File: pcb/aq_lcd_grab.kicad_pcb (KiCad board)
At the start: 4 copper layers, 32 x 50 mm, 41 parts, among them J1 Conn_01x39_Socket, J2 Conn_01x39_Socket, J3 Conn_01x03_Socket, J4 Conn_01x04_Socket, J5 Conn_01x03_Pin, U1 RP2350_60QFN, U2 Conn_01x14, Y1 ABM8-272-T3

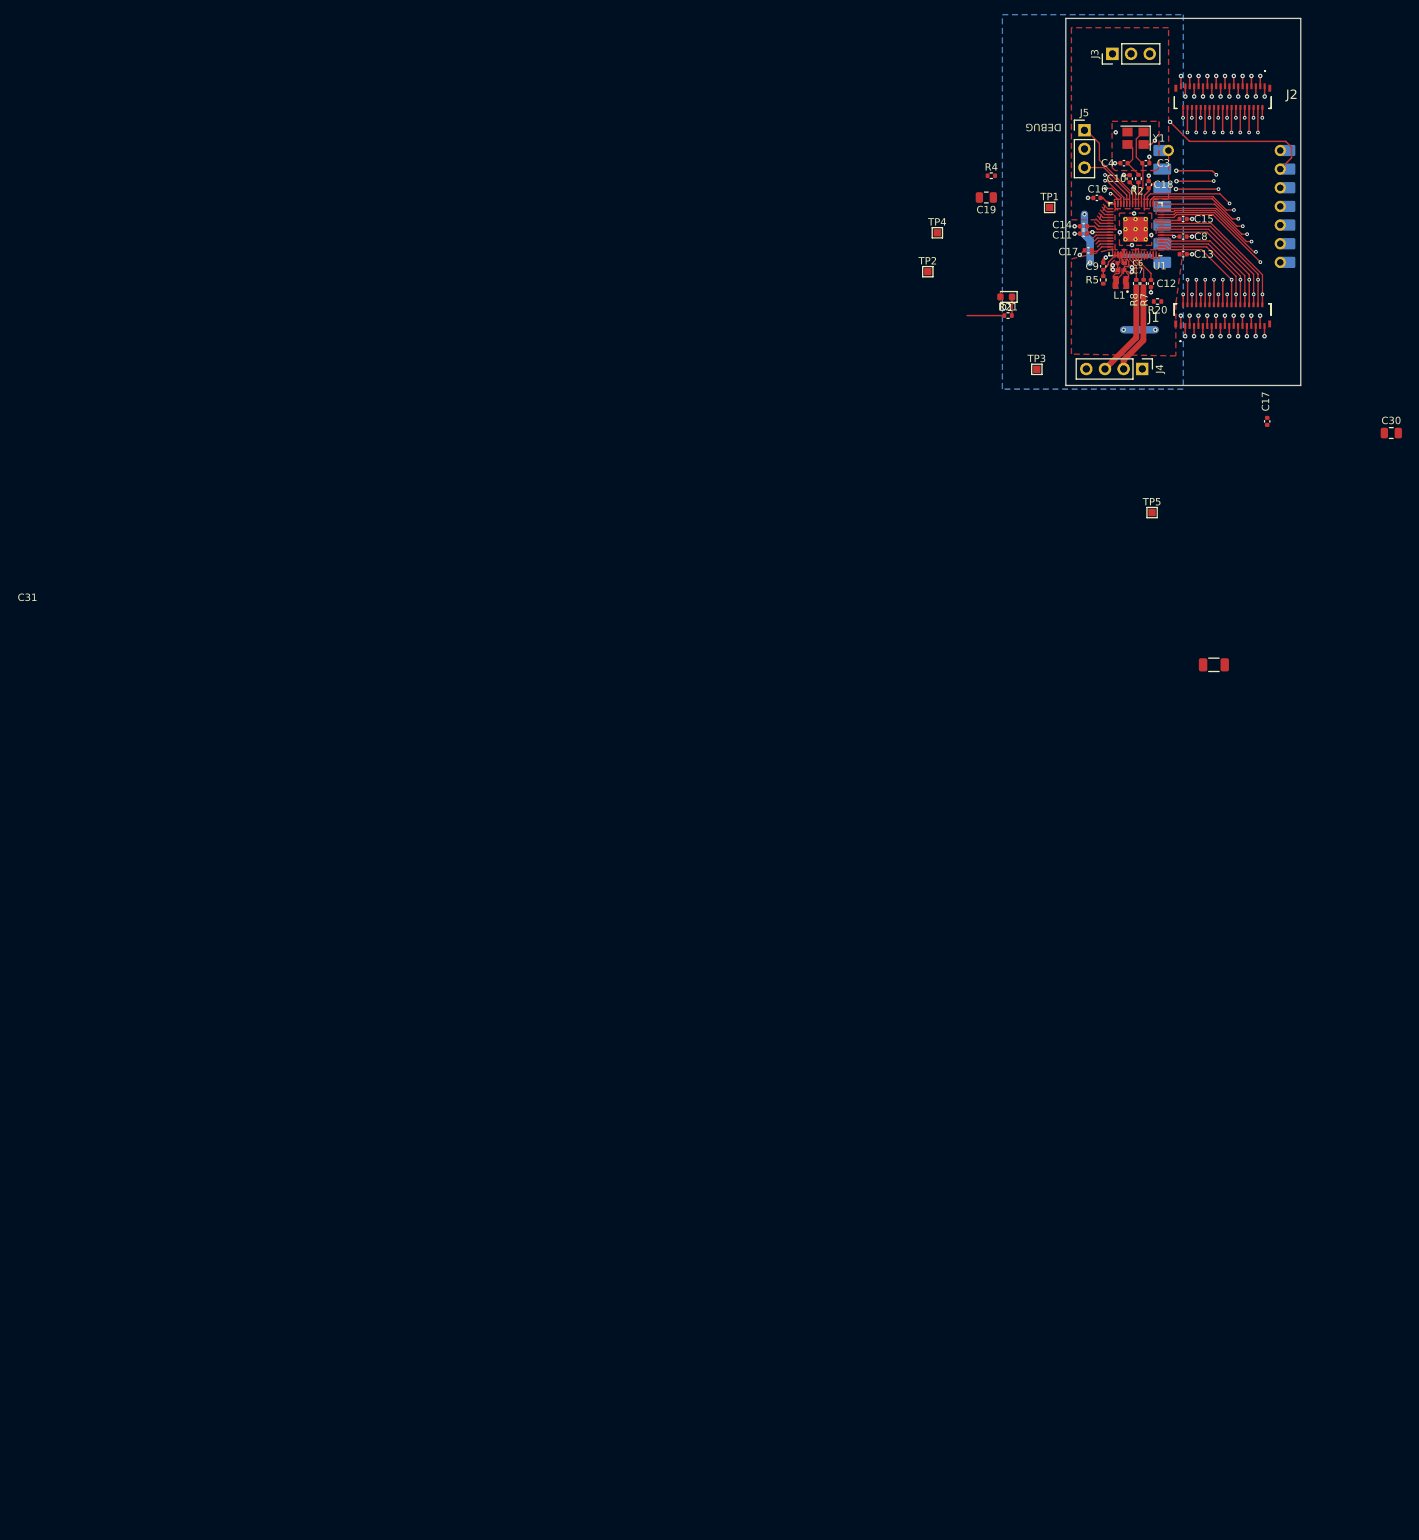
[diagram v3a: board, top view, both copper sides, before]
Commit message: Re-import netlist into PCB
Picks up the smaller test point footprint and the named QSPI strap
nets from the previous commit, plus accumulated layout-side work
from the KiCad session (component placement, routing in progress).

Co-Authored-By: Claude Opus 4.7 (1M context) <noreply@anthropic.com>
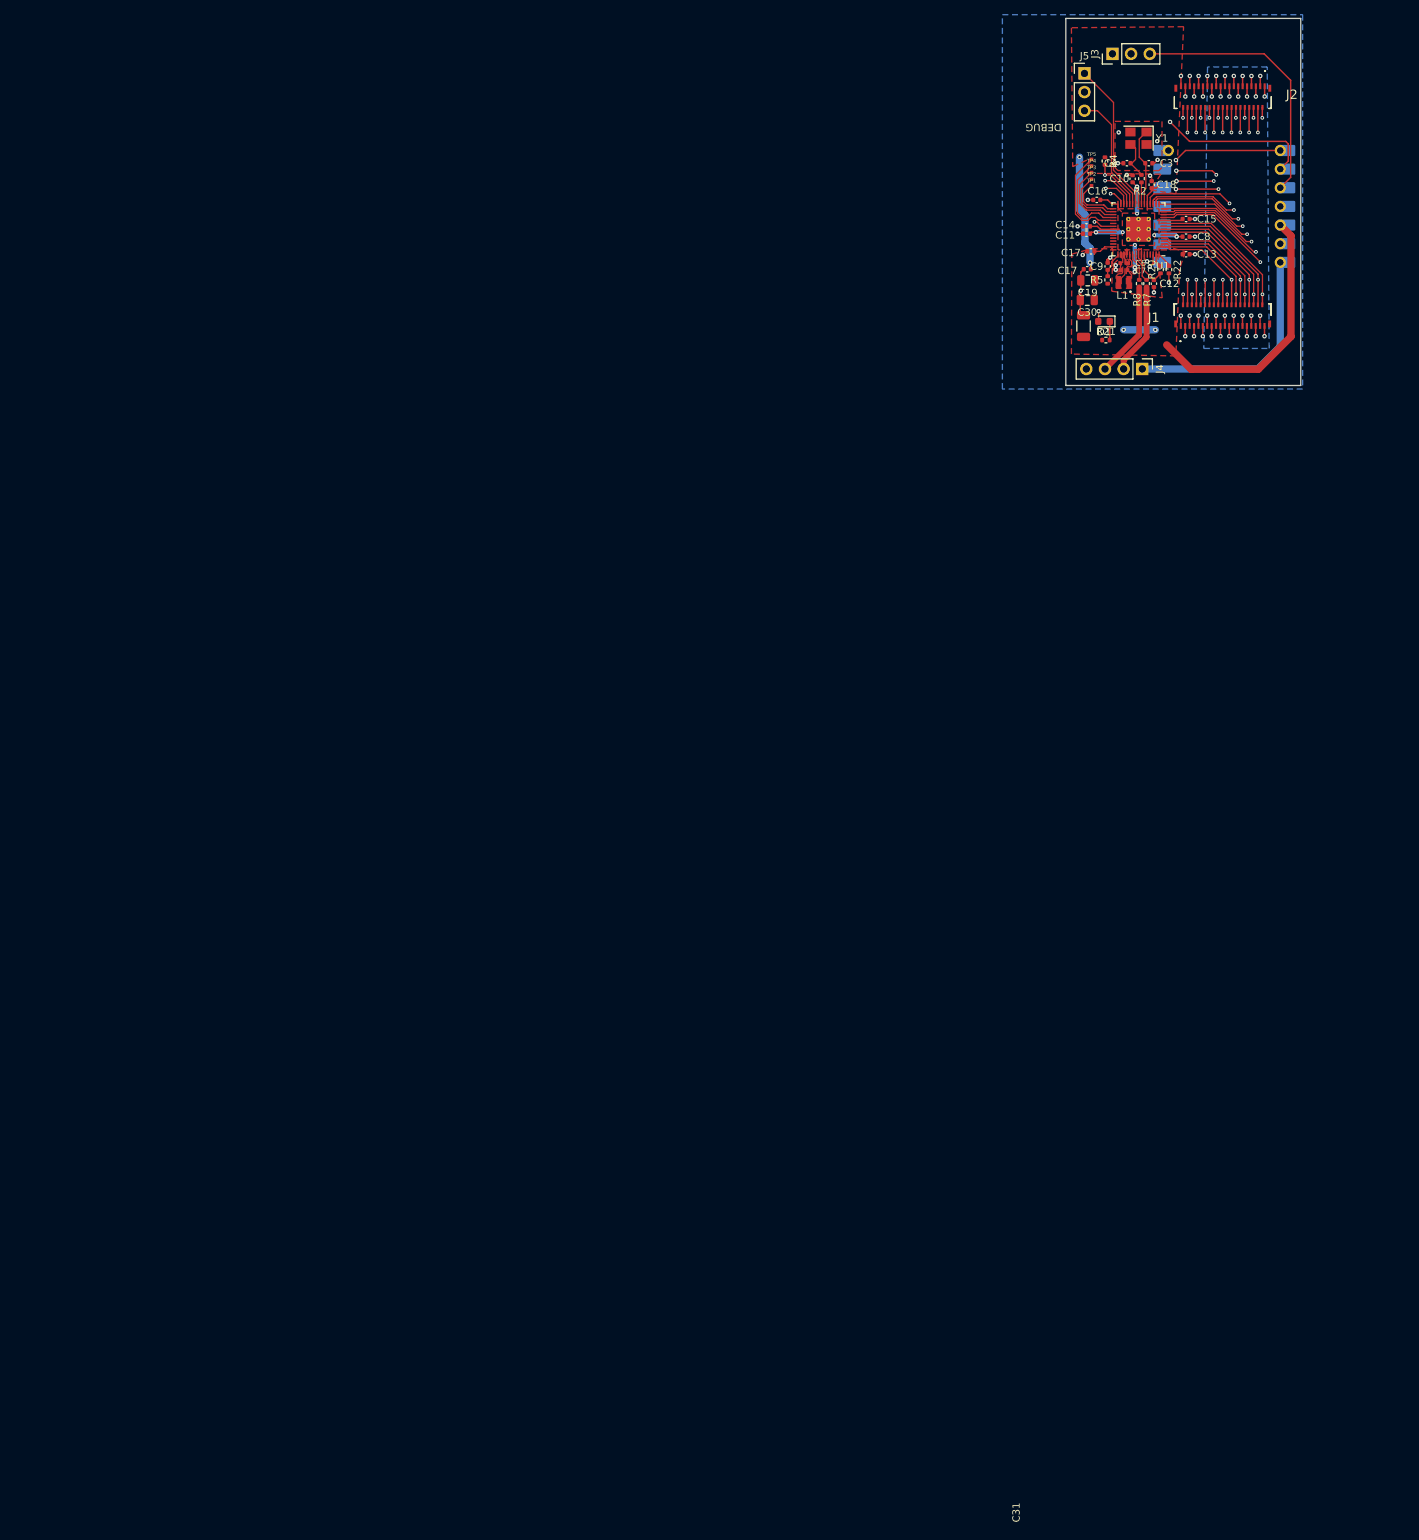
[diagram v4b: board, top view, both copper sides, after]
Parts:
- added R22: 0, Resistor_SMD:R_0402_1005Metric, F.Cu at (64.8, 59.6)
- TP1, TP2, TP3, TP4, TP5: footprint TestPoint:TestPoint_Pad_1.0x1.0mm -> test_points:TestPoint_Pad_0.5x0.5mm
- moved C31 49.4 mm to (53.2, 67.3), turned to 90 degrees
- moved TP5 48.8 mm to (54.3, 44.6)
- moved C30 45.2 mm to (53.7, 63.8), turned to 180 degrees
- moved C17 32.1 mm to (53.7, 59.6), turned to 180 degrees
- moved TP3 27.8 mm to (54.3, 46.4)
- moved TP2 25.6 mm to (54.3, 47.3)
- moved TP4 22.9 mm to (54.3, 45.5)
- moved C19 17.8 mm to (53.8, 61.1)
- moved R4 15.6 mm to (56.1, 44.8), turned to -90 degrees
- moved R21 13.7 mm to (56.3, 69.2)
- moved D1 13.7 mm to (56.0, 66.7)
- moved J5 7.75 mm to (53.3, 32.9)
- moved TP1 6.42 mm to (54.3, 48.2)
- moved R20 4.37 mm to (63.7, 59.6), turned to 90 degrees
- moved C9 0.60 mm to (56.5, 59.2)
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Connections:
- R20 pad 2: N$1 (its old number) -> QSPI_SD1_STRAP
- U1 pad 59: N$1 (its old number) -> QSPI_SD1_STRAP
- U1 pad 60: GND -> QSPI_SS_STRAP
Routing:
- net +3V3: track 41.7 -> 83.7 mm
- net PIC32_RESET: track 0.00 -> 35.9 mm
- net UART_RP_TX: track 0.46 -> 32.6 mm, vias 0 -> 2
- net +5V: track 0.00 -> 31.5 mm
- net UART_RP_RX: track 0.76 -> 17.4 mm, vias 0 -> 1
- net LED_STATUS: track 3.03 -> 16.5 mm, vias 0 -> 2
- net GPIO23: track 2.01 -> 13.8 mm
- net (no net): track 11.1 -> 0.00 mm
- net GPIO22: track 1.81 -> 12.5 mm
- net +1V1: track 14.6 -> 25.1 mm, vias 5 -> 9
- net GPIO21: track 1.61 -> 9.69 mm
- net SWCLK: track 12.9 -> 20.7 mm
- net SWDIO: track 9.07 -> 16.5 mm
- net GPIO20: track 1.36 -> 8.17 mm
- net GPIO19: track 1.21 -> 7.00 mm
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
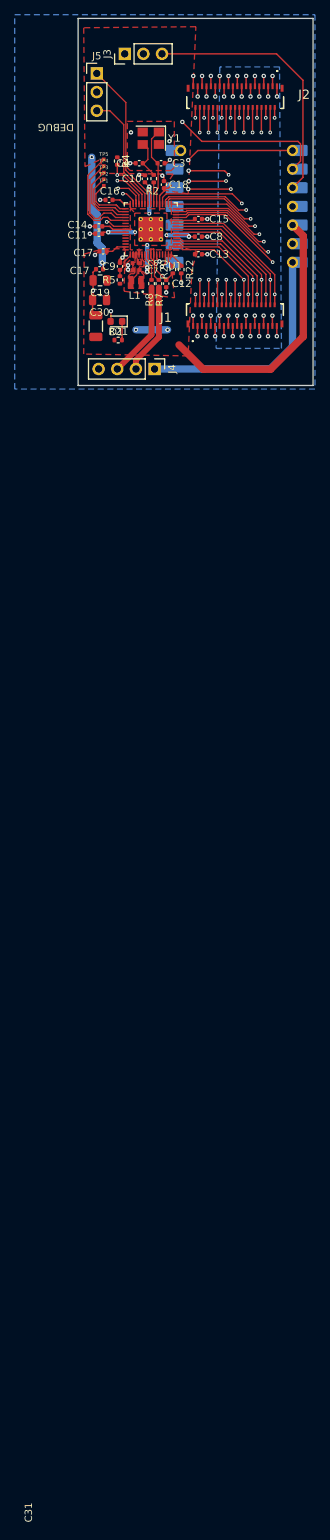
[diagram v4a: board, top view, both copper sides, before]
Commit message: Swap RP2350 for STM32: spec to F103C8T6, PCB rewrite still on F030
docs/pcb_spec.md: rewrite from the RP2350 + flashless UART-boot plan
to STM32. Settle on STM32F103C8T6 after a brief detour through
STM32F030C8T6 (kept as an in-spec addendum for the reasoning trail).
Capture path moves from PIO + DMA ring to TIM1_ETR clocked from WR
with multi-channel DMA reads of GPIOA/GPIOB; channel-to-event
mapping verified against RM0008 Table 78. Pin map handles the F103
specifics: USART1 permanently on PA9/PA10 (bootloader + runtime),
SWD on PA13/PA14, TIM1_ETR on PA12, BOOT1=PB2 forces a pull-down
and moves the status LED off that pin.

pcb/: SKiDL netlist + KiCad PCB + netlist file are an in-progress
F030C8T6 rewrite from a prior session. Committed as-is for history;
they don't yet reflect the F103 decision in the spec and will need
another pass.

.gitignore: stop tracking pcb/production/ fab-output dumps.

Co-Authored-By: Claude Opus 4.7 (1M context) <noreply@anthropic.com>
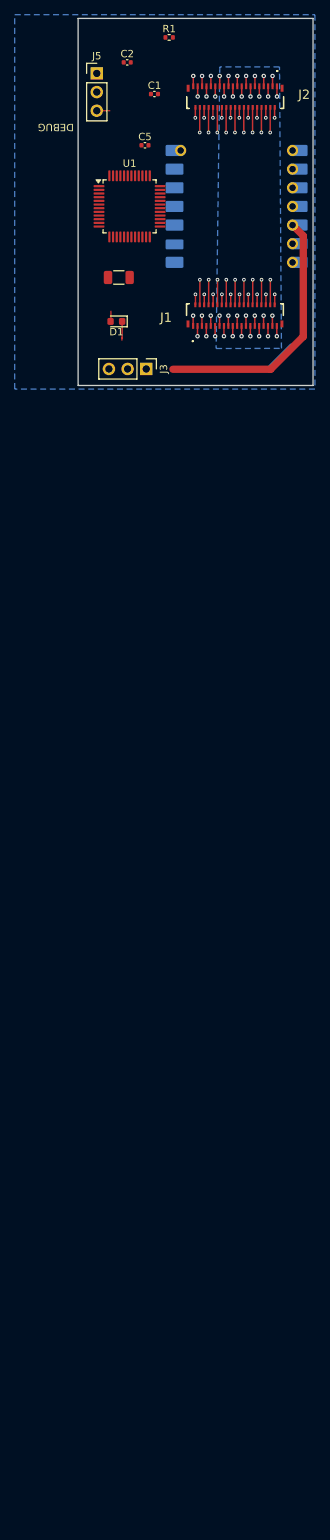
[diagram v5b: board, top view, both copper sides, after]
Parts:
- removed C10, C9: 4.7u, Capacitor_SMD:C_0402_1005Metric
- removed C12, C13, C14, C15, C16, C17 (x2), C18, C8: 100n, Capacitor_SMD:C_0402_1005Metric
- removed C19: 10u, Capacitor_SMD:C_0805_2012Metric
- removed C3, C4: 15p, Capacitor_SMD:C_0402_1005Metric
- removed C30: 22u, Capacitor_SMD:C_0805_2012Metric
- removed C31: 100u, Capacitor_SMD:C_1206_3216Metric
- removed C6, C7: 4.7u, RP2350_60QFN_minimal:C_0402_1005Metric_small_pads
- removed J4: Conn_01x04_Socket, Connector_PinHeader_2.54mm:PinHeader_1x04_P2.54mm_Vertical
- removed L1: 3.3u, RP2350_60QFN_minimal:L_pol_2016
- removed R2, R20, R21, R4: 1k, Resistor_SMD:R_0402_1005Metric
- removed R22: 0, Resistor_SMD:R_0402_1005Metric
- removed R5: 33, Resistor_SMD:R_0402_1005Metric
- removed R7, R8: 27, Resistor_SMD:R_0402_1005Metric
- removed TP1, TP2, TP3, TP4, TP5: TestPoint, test_points:TestPoint_Pad_0.5x0.5mm
- removed Y1: ABM8-272-T3, Crystal:Crystal_SMD_3225-4Pin_3.2x2.5mm
- added C1: 100n, Capacitor_SMD:C_0402_1005Metric, F.Cu at (61.2, 35.7)
- added C2: 100n, Capacitor_SMD:C_0402_1005Metric, F.Cu at (57.5, 31.4)
- added C5: 4.7u, Capacitor_SMD:C_0402_1005Metric, F.Cu at (59.9, 42.7)
- added R1: 10k, Resistor_SMD:R_0402_1005Metric, F.Cu at (63.2, 28.0)
- C11: value 100n -> 100u; footprint Capacitor_SMD:C_0402_1005Metric -> Capacitor_SMD:C_1206_3216Metric
- U1: value RP2350_60QFN -> STM32F030C8Tx; footprint RP2350_60QFN_minimal:RP2350-QFN-60-1EP_7x7_P0.4mm_EP3.4x3.4mm_ThermalVias -> Package_QFP:LQFP-48_7x7mm_P0.5mm
- moved J3 43.0 mm to (60.1, 73.2), turned to -90 degrees
- moved C11 6.56 mm to (56.3, 60.7)
- moved U1 4.25 mm to (57.8, 51.0), turned to 0 degrees
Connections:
- C11 pad 1: +1V1 -> +3V3
- U1 pad 11: +3V3 -> DB1
- U1 pad 12: DB1 -> DB2
- U1 pad 14: DB5 -> DB4
- U1 pad 15: DB7 -> DB5
- U1 pad 16: DB9 -> DB6
- U1 pad 17: DB11 -> DB7
- U1 pad 18: DB13 -> DC
- U1 pad 19: DB15 -> CS
- U1 pad 2: DB14 -> (no net)
- U1 pad 20: +3V3 -> LED_STATUS
- U1 pad 21: XIN -> DB10
- U1 pad 22: XOUT_DRIVE -> DB11
- U1 pad 23: +1V1 -> GND
- U1 pad 24: SWCLK -> +3V3
- U1 pad 25: SWDIO -> DB12
- U1 pad 26: RUN -> DB13
- U1 pad 27: DC -> DB14
- U1 pad 28: CS -> DB15
- U1 pad 29: WR -> (no net)
- U1 pad 3: DB12 -> (no net)
- U1 pad 30: +3V3 -> UART_STM_TX
- U1 pad 31: GPIO19 -> UART_STM_RX
- U1 pad 32: GPIO20 -> (no net)
- U1 pad 33: GPIO21 -> WR
- U1 pad 34: GPIO22 -> SWDIO
- U1 pad 35: GPIO23 -> (no net)
- U1 pad 37: LED_STATUS -> SWCLK
- U1 pad 38: +3V3 -> (no net)
- U1 pad 39: +1V1 -> PB3
- U1 pad 4: DB10 -> (no net)
- U1 pad 40: (no net) -> PB4
- U1 pad 41: (no net) -> PB5
- U1 pad 44: +3V3 -> BOOT0
- U1 pad 45: +3V3 -> DB8
- U1 pad 46: VREG_AVDD -> DB9
- U1 pad 48: VREG_LX -> +3V3
- U1 pad 5: DB8 -> (no net)
- U1 pad 6: +1V1 -> (no net)
- U1 pad 7: DB6 -> NRST
- U1 pad 8: DB4 -> GND
- U1 pad 9: DB2 -> +3V3
- U2 pad 11: (no net) -> BOOT0
- U2 pad 7: UART_RP_RX -> UART_STM_RX
- U2 pad 8: UART_RP_TX -> UART_STM_TX
- U2 pad 9: RUN -> NRST
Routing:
- net +3V3: track 83.7 -> 35.4 mm, vias 4 -> 0
- net RUN: track 45.5 -> 0.00 mm, vias 2 -> 0
- net PIC32_RESET: track 35.9 -> 0.00 mm
- net UART_RP_TX: track 32.6 -> 0.00 mm, vias 2 -> 0
- net +5V: track 31.5 -> 4.31 mm
- net +1V1: track 25.1 -> 0.00 mm, vias 9 -> 0
- net DC: track 59.2 -> 36.4 mm, vias 5 -> 2
- net SWCLK: track 20.7 -> 0.00 mm
- net CS: track 46.5 -> 26.6 mm, vias 5 -> 2
- net DB0: track 46.4 -> 27.0 mm
- net WR: track 45.5 -> 27.0 mm, vias 5 -> 2
- net DB4: track 45.0 -> 27.1 mm
- net UART_RP_RX: track 17.4 -> 0.00 mm, vias 1 -> 0
- net GND: track 17.3 -> 0.00 mm, vias 19 -> 0
- net DB2: track 43.5 -> 26.6 mm
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- removed copper zone on F.Cu, net +1V1
- removed copper zone on F.Cu, net +3V3
- removed copper zone on F.Cu, net GND
- removed copper zone on F.Cu, net VREG_LX
